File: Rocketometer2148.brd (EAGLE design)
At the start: 50.8 x 22.9 mm, 59 parts, among them J001 USB_MICROB_JST, J301 JST 2mm, J401 M06, J701 MICROSD-SOCKET, Q050 PMOS, Q201 PMOS, U101 BMP085, U201 5319, U301 73831, U401 LPC2148, U402 7432, U501 L3G4200D, U601 ADXL345, U801 5883, Y401 12.00

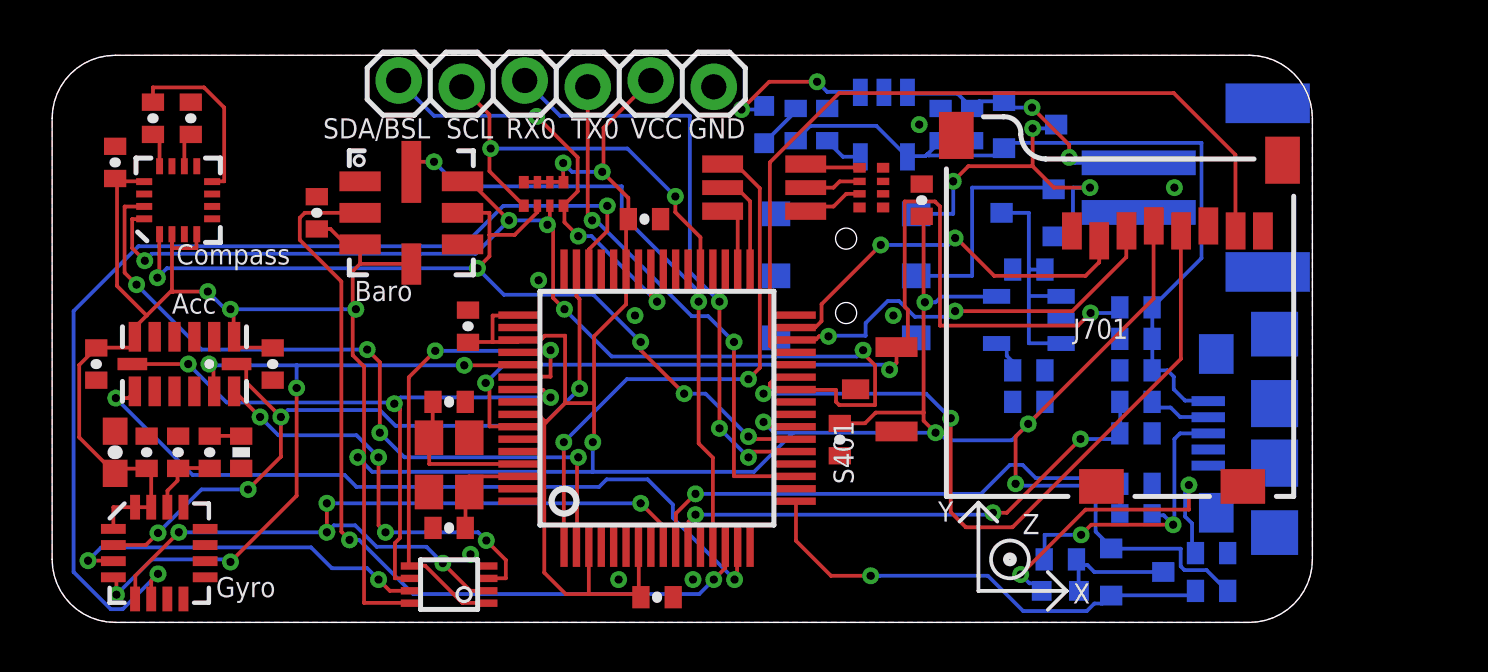
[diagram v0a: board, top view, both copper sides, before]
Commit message: Merged Mio's KwanSystems.lbr, updated all eagle files to use it.
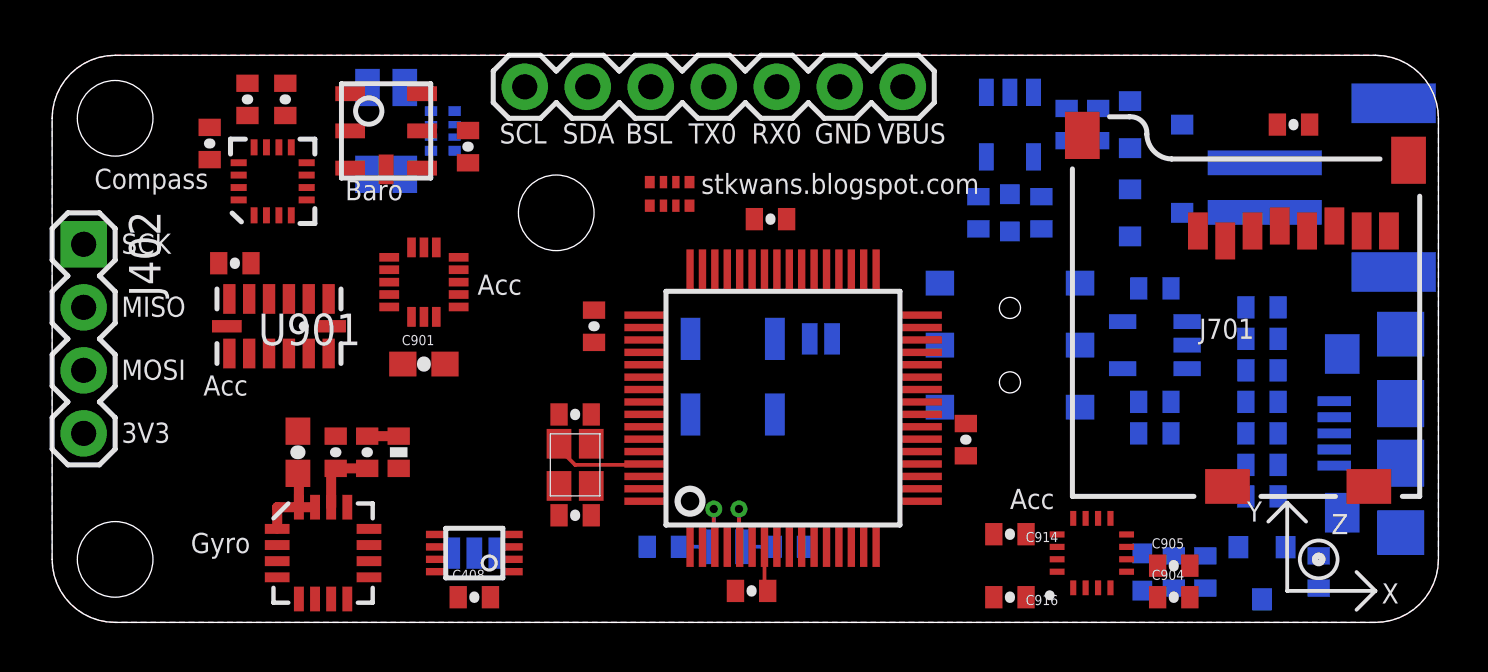
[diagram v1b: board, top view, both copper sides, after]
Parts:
- removed C501, C601: 100nF, SparkFun:0402-CAP
- removed S401: B3U-1100P, KwanSystems:B3U-1100P
- added C403, C405: 22pF, SparkFun:0402-CAP
- added C408, C904, C905, C916: 100nF, SparkFun:0402-CAP
- added C901: 10uF, SparkFun:0603-CAP
- added C914: 4.7uF, SparkFun:0402-CAP
- added J402: M06, SparkFun-Connectors:1X04
- added JP1, JP2, JP3: STAND-OFFTIGHT, SparkFun-Electromechanical:STAND-OFF-TIGHT
- added S403: (no value), SparkFun-Passives:SJ_3
- added S457, S458: B3U-1000P, KwanSystems:B3U-1000P
- added S457A: SOLDERJUMPERNO, SparkFun-Passives:SJ_2S-NO
- added U$2: OSHW-LOGOS, SparkFun-Aesthetics:OSHW-LOGO-S
- added U901: LIS331, KwanSystems:LLGA16
- added U902: AD377, KwanSystems:ADXL377
- added Y402: 32kiHz, KwanSystems:ABS06
- C020, C030, C461, C462: value 18pF -> 22pF
- D401: value GM5WA94310A -> HSMF-C118; device led:GM5WA94310A -> KwanSystems:HSMF-C118
- J401: device SparkFun:1X06_LOCK -> SparkFun-Connectors:1X07
- U101: value BMP085 -> BMP180; device SparkFun:BMP085 -> KwanSystems:BMP180
- Y401: value 12.00 -> 12MHz; device KwanSystems:CRYSTAL_SMD -> KwanSystems:CRYSTAL_SMD_2MM_2_5MM
- moved R402 17.4 mm to (15.7, 19.8), flipped to the bottom, turned to 90 degrees
- moved U$1 15.7 mm to (15.2, 7.11)
- moved D401 15.4 mm to (13.5, 19.8), flipped to the bottom, turned to 90 degrees
- moved C701 15.3 mm to (50.0, 20.1), turned to 0 degrees
- moved R302 10.5 mm to (39.9, 16.5), turned to 90 degrees
- moved D301 10.5 mm to (38.6, 16.5)
- moved J401 7.62 mm to (34.3, 21.6)
- moved C502 7.37 mm to (9.91, 6.86)
- moved S201 7.17 mm to (38.6, 11.2)
- moved R301 7.06 mm to (37.3, 16.5), turned to 90 degrees
- moved C606 6.91 mm to (7.37, 14.5), turned to 0 degrees
- moved C101 6.65 mm to (16.8, 19.2), turned to 270 degrees
- moved U501 6.60 mm to (10.9, 2.79)
- moved R501 6.35 mm to (14.0, 6.86)
- moved C503 6.35 mm to (11.4, 6.86)
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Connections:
- removed net EOC: U101.2, U401.14
- removed net N$12: D401.6, R402.1
- removed net SCL1: J401.5, R401.1, U401.37
- removed net SDA1: J401.6, R401.4, U401.41
- removed net XCLR: U101.8, U401.13
- new net BSL: J401.5, R401.4, U401.41
- new net HACCINT: U401.14, U901.11
- new net N$11: D401.3, R402.1
- new net N$9: D401.2, R402.4
- new net RESET: R401.1, S457.P$1, U401.57
- new net RTXC1: C403.2, U401.3, Y402.2
- new net RTXC2: C405.1, U401.5, Y402.1
- new net XACC: C905.1, U401.38, U902.5
- new net YACC: C904.1, U401.13, U902.4
- new net ZACC: C916.1, U401.39, U902.16
- net AMOSI1: now also S403.1
- net GMOSI1: now also S403.3
- net GND: now also C403.1, C405.2, C408.2, C901.2, C904.2, C905.2, C914.2, C916.2, J401.2, S457A.2, S458.P$2, U101.7, U901.10, U901.12, U901.13, U901.16, U901.5, U901.7, U902.2, U902.6, U902.7; no longer C501.2, C601.2, J401.1, R402.6, R402.7, R402.8, S401.P$2, S401.P$3, U101.1
- net MISO1: now also J402.2
- net MOSI1: now also J402.3, S403.2
- net N$3: now also R402.2; no longer R402.3
- net N$8: now also S457.P$2, S457A.1; no longer D401.5, R402.2
- net PWMB: now also R402.7, U401.34; no longer D401.1, U401.1
- net PWMG: now also R402.5, U401.33; no longer D401.3, U401.34
- net PWMR: now also R402.8, U401.1; no longer D401.2, U401.33
- net RX0: now also J401.3; no longer J401.4
- net SCK1: now also J402.1
- net SCL0: now also J401.7, U101.5, U901.4; no longer U101.6
- net SDA0: now also J401.6, U101.6, U901.6; no longer U101.7
- net TX0: now also J401.4; no longer J401.3
- net USB_ON: now also S458.P$1; no longer S401.P$1
- net VBUS: now also J401.1
- net VCC: now also C408.1, C901.1, C914.1, D401.1, J402.4, U101.2, U901.1, U901.14, U901.15, U901.8, U902.14, U902.15; no longer C501.1, C601.1, J401.2, U101.4, U401.3, U401.57
- net XTAL1: now also Y401.3; no longer Y401.1
- net XTAL2: now also Y401.1; no longer Y401.3
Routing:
- net VCC: track 182.2 -> 6.09 mm, vias 12 -> 0
- net SDA0: track 45.5 -> 0.00 mm, vias 5 -> 0
- net GYROINT: track 42.8 -> 0.00 mm, vias 2 -> 0
- net USB_ON: track 41.1 -> 0.00 mm, vias 3 -> 0
- net SCL0: track 36.9 -> 0.00 mm, vias 5 -> 0
- net EOC: track 33.7 -> 0.00 mm, vias 2 -> 0
- net CSG: track 33.0 -> 0.00 mm, vias 5 -> 0
- net MISO0: track 32.6 -> 0.00 mm
- net VBUS: track 31.4 -> 0.00 mm
- net SCK1: track 31.2 -> 0.00 mm, vias 4 -> 0
- net SCK0: track 30.9 -> 0.00 mm, vias 2 -> 0
- net ACCINT: track 30.8 -> 0.00 mm, vias 2 -> 0
- net COMPINT: track 30.2 -> 0.00 mm, vias 4 -> 0
- net MISO1: track 28.7 -> 0.00 mm, vias 5 -> 0
- net CSA: track 26.9 -> 0.00 mm, vias 3 -> 0
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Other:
- board size 50.8 x 22.9 mm -> 55.9 x 22.9 mm
- board text added: "3V3"
- board text added: "BSL"
- board text added: "Kwan Systems"
- board text added: "MISO"
- board text added: "MOSI"
- board text added: "On"
- board text added: "Rocketometer2148"
- board text added: "SCK"
- board text added: "SDA"
- board text added: "St Kwan's Home for"
- board text added: "VBUS"
- board text added: "a division of"
- board text added: "stkwans.blogspot.com"
- board text added: "the Terminally ADD"
- board text added: "v1.0 25 Dec 2012"
- board text removed: "1 May 2012"
- board text removed: "ON"
- board text removed: "Project Candace"
- board text removed: "SDA/BSL"
- board text removed: "St Kwan's Home for the"
- board text removed: "Stick IMUinator v2.1"
- board text removed: "Terminally ADD"
- board text removed: "VCC"
- board text removed: "a division of Kwan Systems"
